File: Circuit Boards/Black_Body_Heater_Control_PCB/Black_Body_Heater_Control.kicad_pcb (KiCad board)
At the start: 2 copper layers, 57.5 x 42.8 mm, 57 parts, among them J201 5040500891, J202 Conn_01x04_Pin, J203 USB_C_Receptacle_USB2.0_16P, P301 436500200, P302 436500200, Q302 BD139, SW201 SW_MEC_5E, SW202 SW_MEC_5E, U201 AMS1117-3.3, U202 ESP32-S3-WROOM-1-N8R8, U203 USBLC6-2SC6, U301 DAC60501ZDGSR, U302 INA181A2IDBVR, U304 LMR51420XFDDCR, U305 LM358

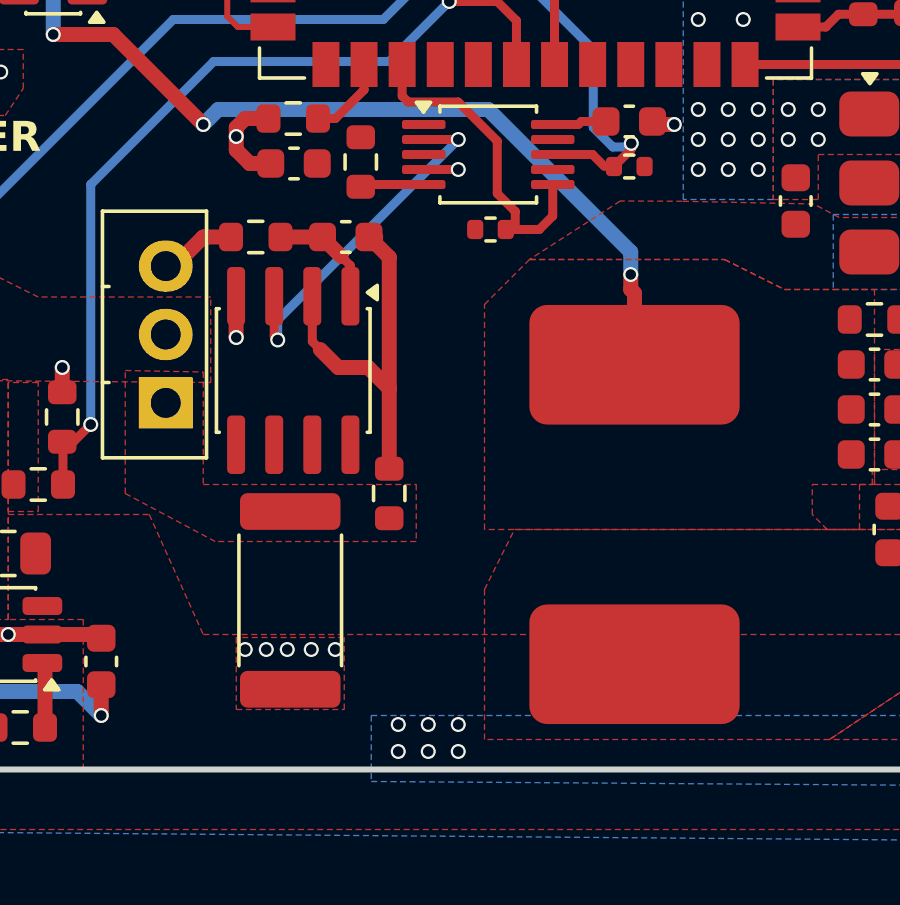
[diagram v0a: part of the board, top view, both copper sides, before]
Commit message: pcb's assembled, test code writen
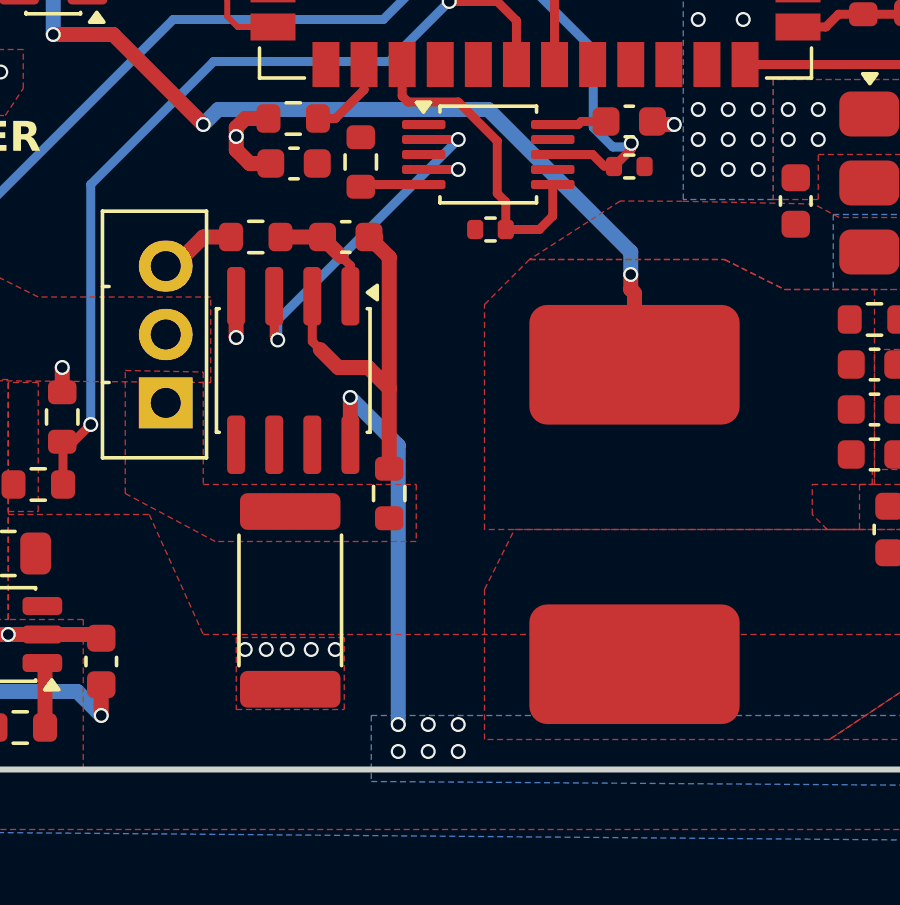
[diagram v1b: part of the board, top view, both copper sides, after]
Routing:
- net VCC: track 2.24 -> 15.4 mm, vias 12 -> 13
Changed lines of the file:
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@@
+	)
+	(segment
+		(start 103.905 110.605)
+		(end 103.9 110.6)
+		(width 0.3)
+		(layer "F.Cu")
+		(net "VCC")
+	)
+	(segment
+		(start 103.905 112.175)
+		(end 103.905 110.605)
+		(width 0.5)
+		(layer "F.Cu")
+		(net "VCC")
 	)
 	(segment
@@
 	)
 	(via
+		(at 103.9 110.6)
+		(size 0.5)
+		(drill 0.35)
+		(layers "F.Cu" "B.Cu")
+		(net "VCC")
+	)
+	(via
 		(at 106.5 121.5)
 		(size 0.5)
@@
 			(back yes)
 		)
+		(net "VCC")
+	)
+	(segment
+		(start 103.9 110.6)
+		(end 105.5 112.2)
+		(width 0.5)
+		(layer "B.Cu")
+		(net "VCC")
+	)
+	(segment
+		(start 105.5 112.2)
+		(end 105.5 121.5)
+		(width 0.5)
+		(layer "B.Cu")
 		(net "VCC")
 	)
@@
 	)
 	(segment
+		(start 103.905 107.225)
+		(end 103.905 106.205)
+		(width 0.3)
+		(layer "F.Cu")
+		(net "/Power_periferals/opamp_out")
+	)
+	(segment
+		(start 103.6 105.9)
+		(end 102.975 105.275)
+		(width 0.5)
+		(layer "F.Cu")
+		(net "/Power_periferals/opamp_out")
+	)
+	(segment
+		(start 102.975 105.25)
+		(end 101.575 105.25)
+		(width 0.5)
+		(layer "F.Cu")
+		(net "/Power_periferals/opamp_out")
+	)
+	(segment
+		(start 103.905 106.205)
+		(end 103.6 105.9)
+		(width 0.3)
+		(layer "F.Cu")
+		(net "/Power_periferals/opamp_out")
+	)
+	(segment
+		(start 102.975 105.275)
+		(end 102.975 105.25)
+		(width 0.5)
+		(layer "F.Cu")
+		(net "/Power_periferals/opamp_out")
+	)
+	(segment
+		(start 103.5 109.6)
+		(end 104.5 109.6)
+		(width 0.5)
+		(layer "F.Cu")
+		(net "/Power_periferals/neg_fdbk")
+	)
+	(segment
+		(start 105.2 110.3)
+		(end 105.2 112.975)
+		(width 0.5)
+		(layer "F.Cu")
+		(net "/Power_periferals/neg_fdbk")
+	)
+	(segment
+		(start 105.2 105.925)
+		(end 105.2 110.3)
+		(width 0.5)
+		(layer "F.Cu")
+		(net "/Power_periferals/neg_fdbk")
+	)
+	(segment
+		(start 104.525 105.25)
+		(end 105.2 105.925)
+		(width 0.5)
+		(layer "F.Cu")
+		(net "/Power_periferals/neg_fdbk")
+	)
+	(segment
+		(start 104.5 109.6)
+		(end 105.2 110.3)
+		(width 0.5)
+		(layer "F.Cu")
+		(net "/Power_periferals/neg_fdbk")
+	)
+	(segment
+		(start 102.635 107.225)
+		(end 102.635 108.735)
+		(width 0.3)
+		(layer "F.Cu")
+		(net "/Power_periferals/neg_fdbk")
+	)
+	(segment
+		(start 104.525 105.25)
+		(end 104.75 105.25)
+		(width 0.5)
+		(layer "F.Cu")
+		(net "/Power_periferals/neg_fdbk")
+	)
+	(segment
+		(start 102.635 108.735)
+		(end 102.9 109)
+		(width 0.3)
+		(layer "F.Cu")
+		(net "/Power_periferals/neg_fdbk")
+	)
+	(segment
+		(start 102.9 109)
+		(end 103.5 109.6)
+		(width 0.5)
+		(layer "F.Cu")
+		(net "/Power_periferals/neg_fdbk")
+	)
+	(segment
+		(start 101.365 108.565)
+		(end 101.5 108.7)
+		(width 0.3)
+		(layer "F.Cu")
+		(net "/Power_periferals/vout")
+	)
+	(segment
+		(start 107.5 102)
+		(end 106.35 102)
+		(width 0.3)
+		(layer "F.Cu")
+		(net "/Power_periferals/vout")
+	)
+	(segment
+		(start 101.5 108.7)
+		(end 101.4825 108.6825)
+		(width 0.3)
+		(layer "F.Cu")
+		(net "/Power_periferals/vout")
+	)
+	(segment
+		(start 101.365 107.225)
+		(end 101.365 108.565)
+		(width 0.3)
+		(layer "F.Cu")
+		(net "/Power_periferals/vout")
+	)
+	(via
+		(at 101.4825 108.6825)
+		(size 0.5)
+		(drill 0.35)
+		(layers "F.Cu" "B.Cu")
+		(net "/Power_periferals/vout")
+	)
+	(via
+		(at 107.5 102)
+		(size 0.5)
+		(drill 0.35)
+		(layers "F.Cu" "B.Cu")
+		(tenting
+			(front yes)
+			(back yes)
+		)
+		(net "/Power_periferals/vout")
+	)
+	(segment
+		(start 101.4825 108.0175)
+		(end 107.5 102)
+		(width 0.3)
+		(layer "B.Cu")
+		(net "/Power_periferals/vout")
+	)
+	(segment
+		(start 101.4825 108.6825)
+		(end 101.4825 108.0175)
+		(width 0.3)
+		(layer "B.Cu")
+		(net "/Power_periferals/vout")
+	)
+	(segment
 		(start 99 105.25)
 		(end 99.925 105.25)
@@
 	)
 	(segment
-		(start 103.905 107.225)
-		(end 103.905 106.205)
-		(width 0.3)
-		(layer "F.Cu")
-		(net "/Power_periferals/opamp_out")
-	)
-	(segment
-		(start 103.6 105.9)
-		(end 102.975 105.275)
-		(width 0.5)
-		(layer "F.Cu")
-		(net "/Power_periferals/opamp_out")
-	)
-	(segment
-		(start 102.975 105.25)
-		(end 101.575 105.25)
-		(width 0.5)
-		(layer "F.Cu")
-		(net "/Power_periferals/opamp_out")
-	)
-	(segment
-		(start 103.905 106.205)
-		(end 103.6 105.9)
-		(width 0.3)
-		(layer "F.Cu")
-		(net "/Power_periferals/opamp_out")
-	)
-	(segment
-		(start 102.975 105.275)
-		(end 102.975 105.25)
-		(width 0.5)
-		(layer "F.Cu")
-		(net "/Power_periferals/opamp_out")
-	)
-	(segment
-		(start 103.5 109.6)
-		(end 104.5 109.6)
-		(width 0.5)
-		(layer "F.Cu")
-		(net "/Power_periferals/neg_fdbk")
-	)
-	(segment
-		(start 105.2 110.3)
-		(end 105.2 112.975)
-		(width 0.5)
-		(layer "F.Cu")
-		(net "/Power_periferals/neg_fdbk")
-	)
-	(segment
-		(start 105.2 105.925)
-		(end 105.2 110.3)
-		(width 0.5)
-		(layer "F.Cu")
-		(net "/Power_periferals/neg_fdbk")
-	)
-	(segment
-		(start 104.525 105.25)
-		(end 105.2 105.925)
-		(width 0.5)
-		(layer "F.Cu")
-		(net "/Power_periferals/neg_fdbk")
-	)
-	(segment
-		(start 104.5 109.6)
-		(end 105.2 110.3)
-		(width 0.5)
-		(layer "F.Cu")
-		(net "/Power_periferals/neg_fdbk")
-	)
-	(segment
-		(start 102.635 107.225)
-		(end 102.635 108.735)
-		(width 0.3)
-		(layer "F.Cu")
-		(net "/Power_periferals/neg_fdbk")
-	)
-	(segment
-		(start 104.525 105.25)
-		(end 104.75 105.25)
-		(width 0.5)
-		(layer "F.Cu")
-		(net "/Power_periferals/neg_fdbk")
-	)
-	(segment
-		(start 102.635 108.735)
-		(end 102.9 109)
-		(width 0.3)
-		(layer "F.Cu")
-		(net "/Power_periferals/neg_fdbk")
-	)
-	(segment
-		(start 102.9 109)
-		(end 103.5 109.6)
-		(width 0.5)
-		(layer "F.Cu")
-		(net "/Power_periferals/neg_fdbk")
-	)
-	(segment
 		(start 96.131251 97.2)
 		(end 96.856251 96.475)
@@
 	)
 	(segment
-		(start 108.8 103.8)
-		(end 109.4 104.4)
+		(start 110.65 104.55)
+		(end 110.65 103.5)
 		(width 0.3)
 		(layer "F.Cu")
@@
 	)
 	(segment
-		(start 110.2 105)
-		(end 109.4 105)
+		(start 108.8 103.8)
+		(end 109.085 104.085)
 		(width 0.3)
 		(layer "F.Cu")
@@
 	)
 	(segment
-		(start 110.65 103.5)
-		(end 110.65 104.55)
+		(start 109.085 104.085)
+		(end 109.085 105)
 		(width 0.3)
 		(layer "F.Cu")
@@
 	)
 	(segment
-		(start 110.65 104.55)
+		(start 109.085 105)
 		(end 110.2 105)
+		(width 0.3)
+		(layer "F.Cu")
+		(net "/ESP32/i2c.scl")
+	)
+	(segment
+		(start 107.5 100.75)
+		(end 108.8 102.05)
+		(width 0.3)
+		(layer "F.Cu")
+		(net "/ESP32/i2c.scl")
+	)
+	(segment
+		(start 105.63 99.5)
+		(end 105.63 100.55)
 		(width 0.3)
 		(layer "F.Cu")
@@
 	)
 	(segment
-		(start 109.4 104.4)
-		(end 109.4 105)
+		(start 110.2 105)
+		(end 110.65 104.55)
 		(width 0.3)
 		(layer "F.Cu")
@@
 	)
 	(segment
-		(start 107.5 100.75)
-		(end 108.8 102.05)
-		(width 0.3)
-		(layer "F.Cu")
-		(net "/ESP32/i2c.scl")
-	)
-	(segment
-		(start 105.63 99.5)
-		(end 105.63 100.55)
-		(width 0.3)
-		(layer "F.Cu")
-		(net "/ESP32/i2c.scl")
-	)
-	(segment
 		(start 108.2 99.47)
 		(end 108.17 99.5)
@@
 	)
 	(segment
-		(start 101.365 108.565)
-		(end 101.5 108.7)
-		(width 0.3)
-		(layer "F.Cu")
-		(net "/Power_periferals/vout")
-	)
-	(segment
-		(start 107.5 102)
-		(end 106.35 102)
-		(width 0.3)
-		(layer "F.Cu")
-		(net "/Power_periferals/vout")
-	)
-	(segment
-		(start 101.5 108.7)
-		(end 101.4825 108.6825)
-		(width 0.3)
-		(layer "F.Cu")
-		(net "/Power_periferals/vout")
-	)
-	(segment
-		(start 101.365 107.225)
-		(end 101.365 108.565)
-		(width 0.3)
-		(layer "F.Cu")
-		(net "/Power_periferals/vout")
-	)
-	(via
-		(at 101.4825 108.6825)
-		(size 0.5)
-		(drill 0.35)
-		(layers "F.Cu" "B.Cu")
-		(net "/Power_periferals/vout")
-	)
-	(via
-		(at 107.5 102)
-		(size 0.5)
-		(drill 0.35)
-		(layers "F.Cu" "B.Cu")
-		(tenting
-			(front yes)
-			(back yes)
-		)
-		(net "/Power_periferals/vout")
-	)
-	(segment
-		(start 101.4825 108.0175)
-		(end 107.5 102)
-		(width 0.3)
-		(layer "B.Cu")
-		(net "/Power_periferals/vout")
-	)
-	(segment
-		(start 101.4825 108.6825)
-		(end 101.4825 108.0175)
-		(width 0.3)
-		(layer "B.Cu")
-		(net "/Power_periferals/vout")
-	)
-	(segment

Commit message: Minor pcb changes
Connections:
- U301 pad 7: unconnected-(U301-~{SYNC}/A0-Pad7) -> /ESP32/i2c.scl
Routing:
- net /ESP32/i2c.scl: track 10.7 -> 11.2 mm
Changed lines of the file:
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@@
 			(layers "F.Cu" "F.Mask" "F.Paste")
 			(roundrect_rratio 0.25)
-			(net "unconnected-(U301-~{SYNC}{slash}A0-Pad7)")
+			(net "/ESP32/i2c.scl")
 			(pinfunction "~{SYNC}/A0_7")
-			(pintype "input+no_connect")
+			(pintype "input")
 		)
 		(pad "8" smd roundrect
@@
 		(width 0.3)
 		(layer "F.Cu")
+		(net "/ESP32/i2c.scl")
+	)
+	(segment
+		(start 110.65 103.5)
+		(end 110.65 103)
+		(width 0.3)
+		(layer "F.Cu")
